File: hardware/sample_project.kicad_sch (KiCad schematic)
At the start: 7 parts

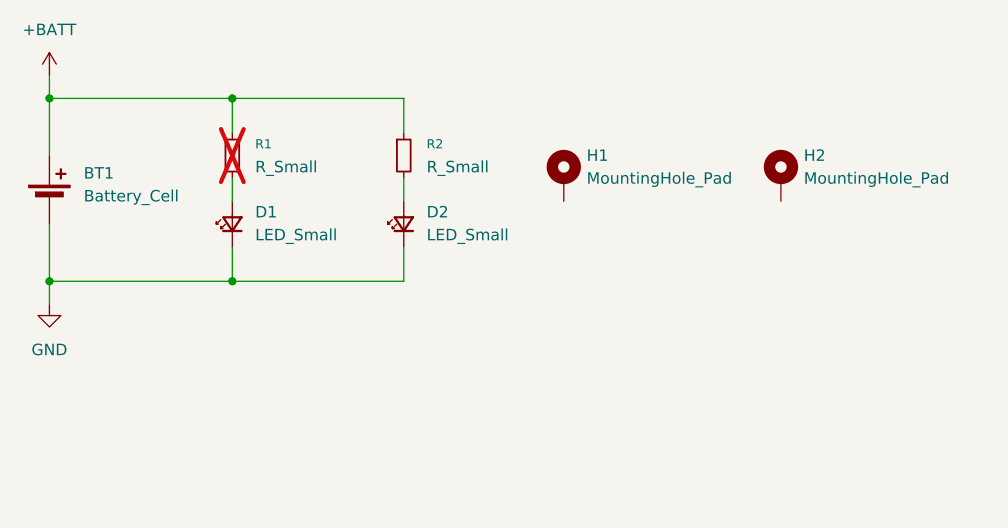
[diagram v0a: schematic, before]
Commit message: bom footprint grouping
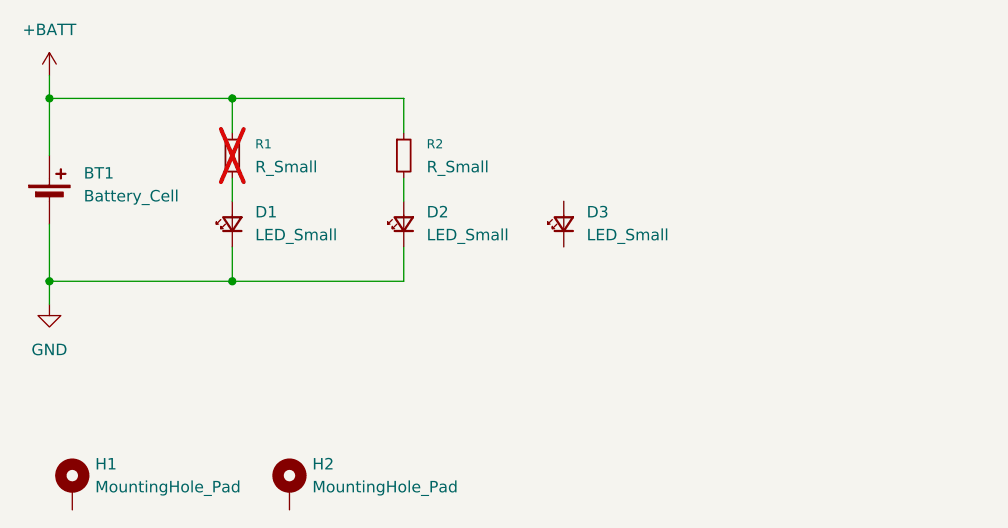
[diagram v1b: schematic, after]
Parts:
- added D3: LED_Small, LED_SMD:LED_0805_2012Metric, symbol Device:LED_Small
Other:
- moved on the sheet: H1, H2
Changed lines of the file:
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@@
 	(symbol
 		(lib_id "Mechanical:MountingHole_Pad")
-		(at 172.72 91.44 0)
+		(at 118.11 125.73 0)
 		(unit 1)
 		(exclude_from_sim no)
@@
 		(fields_autoplaced yes)
 		(property "Reference" "H1"
-			(at 175.26 88.8999 0)
+			(at 120.65 123.1899 0)
 			(effects
 				(font
@@
 		)
 		(property "Value" "MountingHole_Pad"
-			(at 175.26 91.4399 0)
+			(at 120.65 125.7299 0)
 			(effects
 				(font
@@
 		)
 		(property "Footprint" "MountingHole:MountingHole_3.2mm_M3_Pad_Via"
-			(at 172.72 91.44 0)
-			(effects
-				(font
-					(size 1.27 1.27)
-				)
-				(hide yes)
-			)
-		)
-		(property "Datasheet" "~"
-			(at 172.72 91.44 0)
+			(at 118.11 125.73 0)
+			(effects
+				(font
+					(size 1.27 1.27)
+				)
+				(hide yes)
+			)
+		)
+		(property "Datasheet" "~"
+			(at 118.11 125.73 0)
 			(effects
 				(font
@@
 		)
 		(property "Description" "Mounting Hole with connection"
-			(at 172.72 91.44 0)
+			(at 118.11 125.73 0)
 			(effects
 				(font
@@
 	(symbol
 		(lib_id "Mechanical:MountingHole_Pad")
-		(at 196.85 91.44 0)
+		(at 142.24 125.73 0)
 		(unit 1)
 		(exclude_from_sim no)
@@
 		(fields_autoplaced yes)
 		(property "Reference" "H2"
-			(at 199.39 88.8999 0)
+			(at 144.78 123.1899 0)
 			(effects
 				(font
@@
 		)
 		(property "Value" "MountingHole_Pad"
-			(at 199.39 91.4399 0)
+			(at 144.78 125.7299 0)
 			(effects
 				(font
@@
 		)
 		(property "Footprint" "MountingHole:MountingHole_3.2mm_M3_Pad_Via"
-			(at 196.85 91.44 0)
-			(effects
-				(font
-					(size 1.27 1.27)
-				)
-				(hide yes)
-			)
-		)
-		(property "Datasheet" "~"
-			(at 196.85 91.44 0)
+			(at 142.24 125.73 0)
+			(effects
+				(font
+					(size 1.27 1.27)
+				)
+				(hide yes)
+			)
+		)
+		(property "Datasheet" "~"
+			(at 142.24 125.73 0)
 			(effects
 				(font
@@
 		)
 		(property "Description" "Mounting Hole with connection"
-			(at 196.85 91.44 0)
+			(at 142.24 125.73 0)
 			(effects
 				(font
@@
 					(unit 1)
 				)
+			)
+		)
+	)
+	(symbol
+		(lib_id "Device:LED_Small")
+		(at 172.72 96.52 90)
+		(unit 1)
+		(exclude_from_sim no)
+		(in_bom yes)
+		(on_board yes)
+		(dnp no)
+		(fields_autoplaced yes)
+		(property "Reference" "D3"
+			(at 175.26 95.1864 90)
+			(effects
+				(font
+					(size 1.27 1.27)
+				)
+				(justify right)
+			)
+		)
+		(property "Value" "LED_Small"
+			(at 175.26 97.7264 90)
+			(effects
+				(font
+					(size 1.27 1.27)
+				)
+				(justify right)
+			)
+		)
+		(property "Footprint" "LED_SMD:LED_0805_2012Metric"
+			(at 172.72 96.52 90)
+			(effects
+				(font
+					(size 1.27 1.27)
+				)
+				(hide yes)
+			)
+		)
+		(property "Datasheet" "~"
+			(at 172.72 96.52 90)
+			(effects
+				(font
+					(size 1.27 1.27)
+				)
+				(hide yes)
+			)
+		)
+		(property "Description" "Light emitting diode, small symbol"
+			(at 172.72 96.52 0)
+			(effects
+				(font
+					(size 1.27 1.27)
+				)
+				(hide yes)
+			)
+		)
+		(property "Sim.Pin" "1=K 2=A"
+			(at 172.72 96.52 0)
+			(effects
+				(font
+					(size 1.27 1.27)
+				)
+				(hide yes)
+			)
+		)
+		(pin "1"
+		)
+		(pin "2"
+		)
+		(instances
+			(project "sample_project"
+				(path "/0b85b844-2f62-47f8-85c0-b274be88892e"
+					(reference "D3")
+					(unit 1)
+				)
